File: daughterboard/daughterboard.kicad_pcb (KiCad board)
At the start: 2 copper layers, 150 x 51.8 mm, 15 parts, among them J1 Conn_01x30, J2 Conn_01x02_Female, U1 YAAJ_WeAct_BlackPill_Part_Lik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

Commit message: Daughterboard updates
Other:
- rule pad_to_mask_clearance: 0.0508 -> 0
- board text added: "Daughterboard (Rev 1) Designed by dcpedit github.com/dcpedit/mod-mmm"
- board text removed: "(Rev 1) Designed by dcpedit github.com/dcpedit/mod-mmm"
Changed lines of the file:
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@@
       (dielectric_constraints no)
     )
-    (pad_to_mask_clearance 0.0508)
-    (solder_mask_min_width 0.101)
+    (pad_to_mask_clearance 0)
     (aux_axis_origin 64.77 46.99)
     (grid_origin 64.77 46.99)
@@
       (layerselection 0x00010fc_ffffffff)
       (disableapertmacros false)
-      (usegerberextensions false)
+      (usegerberextensions true)
       (usegerberattributes false)
       (usegerberadvancedattributes false)
@@
       (psa4output false)
       (plotreference true)
-      (plotvalue true)
+      (plotvalue false)
       (plotinvisibletext false)
       (sketchpadsonfab false)
-      (subtractmaskfromsilk false)
+      (subtractmaskfromsilk true)
       (outputformat 1)
       (mirror false)
@@
       (effects (font (size 0.5 0.5) (thickness 0.1)))
     )
-    (fp_text user "REF**" (at 7.62 24.13 90) (layer "F.Fab")
+    (fp_text user "REF**" (at 7.62 24.13 90) (layer "F.Fab") hide
       (effects (font (size 1 1) (thickness 0.15)))
     )
@@
   (gr_arc (start 76.454 96.99) (mid 76.992815 97.213185) (end 77.216 97.752) (layer "Edge.Cuts") (width 0.05))
   (gr_line (start 77.216 97.752) (end 77.216 98.044) (layer "Edge.Cuts") (width 0.05))
-  (gr_text "  (Rev 1)\n Designed by dcpedit\ngithub.com/dcpedit/mod-mmm" (at 154.686 92.583) (layer "F.SilkS")
+  (gr_text "  Daughterboard (Rev 1)\n Designed by dcpedit\ngithub.com/dcpedit/mod-mmm" (at 154.686 92.583) (layer "F.SilkS")
     (effects (font (size 1 1) (thickness 0.15)) (justify left))
   )

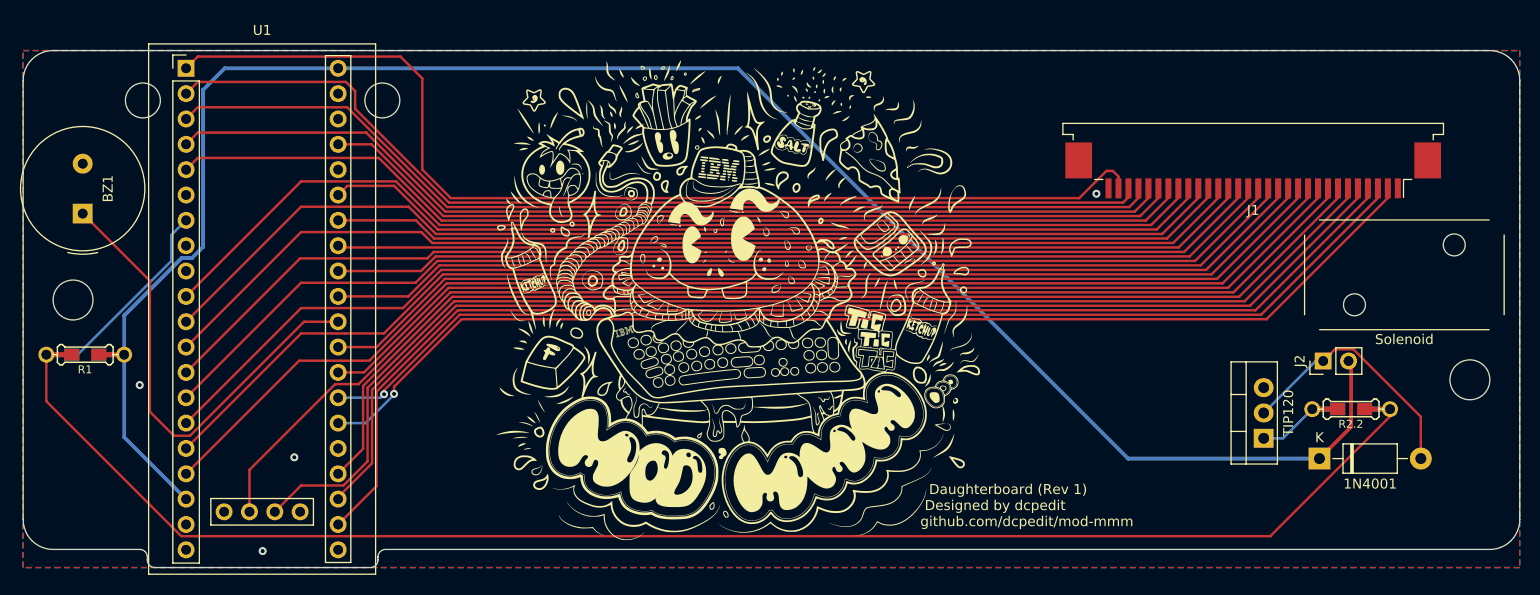
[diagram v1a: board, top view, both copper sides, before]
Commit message: daughterboard rewire
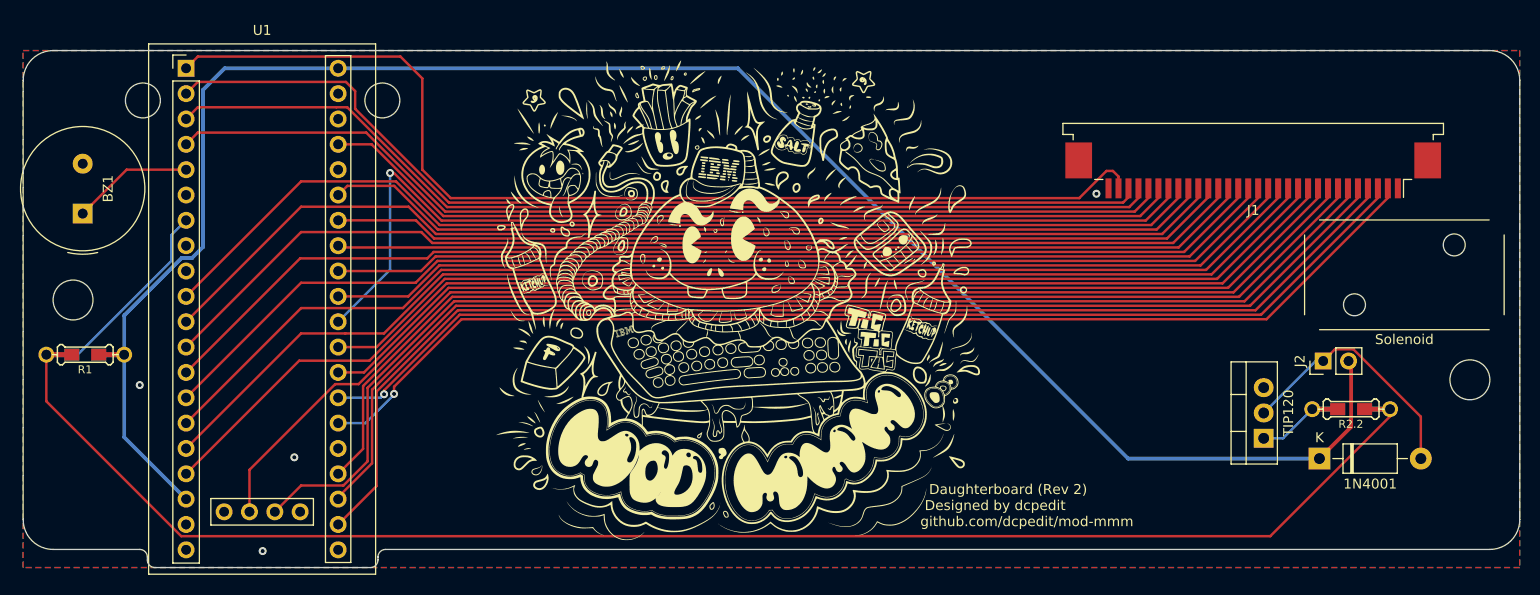
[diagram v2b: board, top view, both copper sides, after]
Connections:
- U1 pad 30: BUZ -> ROW6
- U1 pad 44: /3V3 -> unconnected-(U1-Pad44)
- U1 pad 5: ROW6 -> BUZ
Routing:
- net BUZ: track 47.2 -> 12.2 mm
- net ROW6: track 103.4 -> 98.9 mm, vias 0 -> 1
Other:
- board text added: "Daughterboard (Rev 2) Designed by dcpedit github.com/dcpedit/mod-mmm"
- board text removed: "Daughterboard (Rev 1) Designed by dcpedit github.com/dcpedit/mod-mmm"
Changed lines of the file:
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@@
   (net 1 "GND")
   (net 2 "+5V")
-  (net 3 "Net-(J2-Pad1)")
+  (net 3 "Net-(1N4001-Pad2)")
   (net 4 "BUZ")
   (net 5 "SCRL_LED")
@@
   (net 32 "CAPS_LED")
   (net 33 "SOL")
-  (net 34 "Net-(TIP120-Pad1)")
+  (net 34 "Net-(R2.2-Pad2)")
   (net 35 "unconnected-(U1-Pad38)")
   (net 36 "unconnected-(U1-Pad36)")
@@
   (net 41 "unconnected-(U1-Pad21)")
   (net 42 "unconnected-(U1-Pad20)")
-  (net 43 "/3V3")
+  (net 43 "unconnected-(U1-Pad44)")
   (footprint "MountingHole:MountingHole_3.5mm" locked (layer "F.Cu")
     (at 76.77 51.99)
@@
       (net 2 "+5V") (pinfunction "K") (pintype "passive"))
     (pad "2" thru_hole oval (at 10.16 0) (size 2.2 2.2) (drill 1.1) (layers *.Cu *.Mask)
-      (net 3 "Net-(J2-Pad1)") (pinfunction "A") (pintype "passive"))
+      (net 3 "Net-(1N4001-Pad2)") (pinfunction "A") (pintype "passive"))
     (model "${KICAD6_3DMODEL_DIR}/Diode_THT.3dshapes/D_DO-41_SOD81_P10.16mm_Horizontal.wrl"
       (offset (xyz 0 0 0))
@@
     (fp_line (start -2.46 1.25) (end 7.54 1.25) (layer "F.Fab") (width 0.1))
     (pad "1" thru_hole rect (at 0 0 90) (size 1.905 2) (drill 1.1) (layers *.Cu *.Mask)
-      (net 34 "Net-(TIP120-Pad1)") (pinfunction "B") (pintype "input"))
+      (net 34 "Net-(R2.2-Pad2)") (pinfunction "B") (pintype "input"))
     (pad "2" thru_hole oval (at 2.54 0 90) (size 1.905 2) (drill 1.1) (layers *.Cu *.Mask)
-      (net 3 "Net-(J2-Pad1)") (pinfunction "C") (pintype "passive"))
+      (net 3 "Net-(1N4001-Pad2)") (pinfunction "C") (pintype "passive"))
     (pad "3" thru_hole oval (at 5.08 0 90) (size 1.905 2) (drill 1.1) (layers *.Cu *.Mask)
       (net 1 "GND") (pinfunction "E") (pintype "passive"))
@@
     (fp_line (start -0.635 -1.27) (end 1.27 -1.27) (layer "F.Fab") (width 0.1))
     (pad "1" thru_hole rect (at 0 0 90) (size 1.7 1.7) (drill 1) (layers *.Cu *.Mask)
-      (net 3 "Net-(J2-Pad1)") (pinfunction "Pin_1") (pintype "passive"))
+      (net 3 "Net-(1N4001-Pad2)") (pinfunction "Pin_1") (pintype "passive"))
     (pad "2" thru_hole oval (at 0 2.54 90) (size 1.7 1.7) (drill 1) (layers *.Cu *.Mask)
       (net 2 "+5V") (pinfunction "Pin_2") (pintype "passive"))
@@
       (net 29 "COL2") (pinfunction "PB15") (pintype "bidirectional"))
     (pad "5" thru_hole circle locked (at 0 10.16) (size 1.7 1.7) (drill 1) (layers *.Cu *.Mask)
-      (net 27 "ROW6") (pinfunction "PA8") (pintype "bidirectional"))
+      (net 4 "BUZ") (pinfunction "PA8") (pintype "bidirectional"))
     (pad "6" thru_hole circle locked (at 0 12.7) (size 1.7 1.7) (drill 1) (layers *.Cu *.Mask)
       (net 37 "unconnected-(U1-Pad6)") (pinfunction "PA9") (pintype "bidirectional+no_connect"))
@@
       (net 14 "COL5") (pinfunction "PA3") (pintype "bidirectional"))
     (pad "30" thru_hole circle locked (at 15.24 25.4) (size 1.7 1.7) (drill 1) (layers *.Cu *.Mask)
-      (net 4 "BUZ") (pinfunction "PA4") (pintype "bidirectional"))
+      (net 27 "ROW6") (pinfunction "PA4") (pintype "bidirectional"))
     (pad "31" thru_hole circle locked (at 15.24 22.86) (size 1.7 1.7) (drill 1) (layers *.Cu *.Mask)
       (net 17 "ROW9") (pinfunction "PA5") (pintype "bidirectional"))
@@
       (net 11 "RE2") (pinfunction "SWIO") (pintype "bidirectional"))
     (pad "44" thru_hole circle locked (at 3.812 44.449) (size 1.7 1.7) (drill 1) (layers *.Cu *.Mask)
-      (net 43 "/3V3") (pinfunction "3V3") (pintype "power_in"))
+      (net 43 "unconnected-(U1-Pad44)") (pinfunction "3V3") (pintype "power_in+no_connect"))
     (model "D:/Users/admin/Documents/KiCad/Libraries/packages3d/Modules/STM32_Blue_Pill/YAAJ_BluePill_PinHeaders_H_SWD_cp.wrl"
       (offset (xyz 0 0 0))
@@
       (net 33 "SOL") (pintype "passive") (solder_mask_margin -999))
     (pad "2" smd rect locked (at -2.5 0) (size 2.9 0.5) (layers "B.Cu")
-      (net 34 "Net-(TIP120-Pad1)") (pintype "passive") (solder_mask_margin -999))
+      (net 34 "Net-(R2.2-Pad2)") (pintype "passive") (solder_mask_margin -999))
     (pad "2" smd rect locked (at -1.35 0) (size 1.5 1.2) (layers "F.Cu" "F.Paste" "F.Mask")
-      (net 34 "Net-(TIP120-Pad1)") (pintype "passive"))
+      (net 34 "Net-(R2.2-Pad2)") (pintype "passive"))
     (pad "2" smd rect locked (at -1.35 0) (size 1.5 1.2) (layers "B.Cu" "B.Paste" "B.Mask")
-      (net 34 "Net-(TIP120-Pad1)") (pintype "passive"))
+      (net 34 "Net-(R2.2-Pad2)") (pintype "passive"))
     (pad "2" thru_hole circle locked (at -3.9 0) (size 1.6 1.6) (drill 1) (layers *.Cu *.Mask "F.SilkS")
-      (net 34 "Net-(TIP120-Pad1)") (pintype "passive"))
+      (net 34 "Net-(R2.2-Pad2)") (pintype "passive"))
     (pad "2" smd rect locked (at -2.5 0) (size 2.9 0.5) (layers "F.Cu")
-      (net 34 "Net-(TIP120-Pad1)") (pintype "passive") (solder_mask_margin -999))
+      (net 34 "Net-(R2.2-Pad2)") (pintype "passive") (solder_mask_margin -999))
     (model "${KICAD6_3DMODEL_DIR}/Resistors_SMD.3dshapes/R_0805.step"
       (offset (xyz 0 0 0))
@@
   (gr_arc (start 76.454 96.99) (mid 76.992815 97.213185) (end 77.216 97.752) (layer "Edge.Cuts") (width 0.05))
   (gr_line (start 77.216 97.752) (end 77.216 98.044) (layer "Edge.Cuts") (width 0.05))
-  (gr_text "  Daughterboard (Rev 1)\n Designed by dcpedit\ngithub.com/dcpedit/mod-mmm" (at 154.686 92.583) (layer "F.SilkS")
+  (gr_text "  Daughterboard (Rev 2)\n Designed by dcpedit\ngithub.com/dcpedit/mod-mmm" (at 154.686 92.583) (layer "F.SilkS")
     (effects (font (size 1 1) (thickness 0.15)) (justify left))
   )
@@
   (segment (start 194.31 78.105) (end 195.067 78.105) (width 0.25) (layer "B.Cu") (net 3))
   (segment (start 189.103 83.312) (end 194.31 78.105) (width 0.25) (layer "B.Cu") (net 3))
-  (segment (start 77.47 70.061785) (end 70.739 63.330785) (width 0.25) (layer "F.Cu") (net 4))
-  (segment (start 96.34 74.168) (end 92.92101 74.168) (width 0.25) (layer "F.Cu") (net 4))
-  (segment (start 92.92101 74.168) (end 81.49101 85.598) (width 0.25) (layer "F.Cu") (net 4))
-  (segment (start 79.883 85.598) (end 77.47 83.185) (width 0.25) (layer "F.Cu") (net 4))
-  (segment (start 77.47 83.185) (end 77.47 70.061785) (width 0.25) (layer "F.Cu") (net 4))
-  (segment (start 81.49101 85.598) (end 79.883 85.598) (width 0.25) (layer "F.Cu") (net 4))
+  (segment (start 75.141785 58.928) (end 70.739 63.330785) (width 0.25) (layer "F.Cu") (net 4))
+  (segment (start 81.1 58.928) (end 75.141785 58.928) (width 0.25) (layer "F.Cu") (net 4))
   (segment (start 201.55 61.754022) (end 201.55 60.8) (width 0.25) (layer "F.Cu") (net 5))
   (segment (start 189.386503 73.917519) (end 201.55 61.754022) (width 0.25) (layer "F.Cu") (net 5))
@@
   (segment (start 177.826422 64.4776) (end 180.55 61.754022) (width 0.25) (layer "F.Cu") (net 26))
   (segment (start 106.512449 64.4776) (end 177.826422 64.4776) (width 0.25) (layer "F.Cu") (net 26))
-  (segment (start 177.275942 64.02808) (end 179.55 61.754022) (width 0.25) (layer "F.Cu") (net 27))
-  (segment (start 82.274511 57.753489) (end 100.424053 57.753489) (width 0.25) (layer "F.Cu") (net 27))
-  (segment (start 81.1 58.928) (end 82.274511 57.753489) (width 0.25) (layer "F.Cu") (net 27))
-  (segment (start 106.698646 64.02808) (end 177.275942 64.02808) (width 0.25) (layer "F.Cu") (net 27))
-  (segment (start 100.424053 57.753489) (end 106.698646 64.02808) (width 0.25) (layer "F.Cu") (net 27))
+  (segment (start 101.543609 59.261924) (end 101.932488 59.261924) (width 0.25) (layer "F.Cu") (net 27))
   (segment (start 179.55 61.754022) (end 179.55 60.8) (width 0.25) (layer "F.Cu") (net 27))
+  (segment (start 106.698646 64.02808) (end 177.275942 64.02808) (width 0.25) (layer "F.Cu") (net 27))
+  (segment (start 177.275942 64.02808) (end 179.55 61.754022) (width 0.25) (layer "F.Cu") (net 27))
+  (segment (start 101.932488 59.261924) (end 106.698646 64.02808) (width 0.25) (layer "F.Cu") (net 27))
+  (via (at 101.543609 59.261924) (size 0.8) (drill 0.4) (layers "F.Cu" "B.Cu") (net 27))
+  (segment (start 96.34 74.168) (end 101.543609 68.964391) (width 0.25) (layer "B.Cu") (net 27))
+  (segment (start 101.543609 68.964391) (end 101.543609 59.261924) (width 0.25) (layer "B.Cu") (net 27))
   (segment (start 99.694282 56.388) (end 106.884843 63.57856) (width 0.25) (layer "F.Cu") (net 28))
   (segment (start 106.884843 63.57856) (end 176.725462 63.57856) (width 0.25) (layer "F.Cu") (net 28))

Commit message: v3 with 10u support
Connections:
- U1 pad 41: GND -> unconnected-(U1-Pad41)
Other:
- board text added: "Daughterboard (Rev 2.1) Designed by dcpedit github.com/dcpedit/mod-mmm"
- board text removed: "Daughterboard (Rev 2) Designed by dcpedit github.com/dcpedit/mod-mmm"
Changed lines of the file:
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@@
   (net 42 "unconnected-(U1-Pad20)")
   (net 43 "unconnected-(U1-Pad44)")
+  (net 44 "unconnected-(U1-Pad41)")
   (footprint "MountingHole:MountingHole_3.5mm" locked (layer "F.Cu")
     (at 76.77 51.99)
@@
       (net 2 "+5V") (pinfunction "5V") (pintype "power_in"))
     (pad "41" thru_hole circle locked (at 11.432 44.449) (size 1.7 1.7) (drill 1) (layers *.Cu *.Mask)
-      (net 1 "GND") (pinfunction "GND") (pintype "power_in"))
+      (net 44 "unconnected-(U1-Pad41)") (pinfunction "GND") (pintype "power_in+no_connect"))
     (pad "42" thru_hole circle locked (at 8.892 44.449) (size 1.7 1.7) (drill 1) (layers *.Cu *.Mask)
       (net 9 "RE3") (pinfunction "SWCLK") (pintype "bidirectional"))
@@
   (gr_arc (start 76.454 96.99) (mid 76.992815 97.213185) (end 77.216 97.752) (layer "Edge.Cuts") (width 0.05))
   (gr_line (start 77.216 97.752) (end 77.216 98.044) (layer "Edge.Cuts") (width 0.05))
-  (gr_text "  Daughterboard (Rev 2)\n Designed by dcpedit\ngithub.com/dcpedit/mod-mmm" (at 154.686 92.583) (layer "F.SilkS")
+  (gr_text "  Daughterboard (Rev 2.1)\n Designed by dcpedit\ngithub.com/dcpedit/mod-mmm" (at 154.686 92.583) (layer "F.SilkS")
     (effects (font (size 1 1) (thickness 0.15)) (justify left))
   )

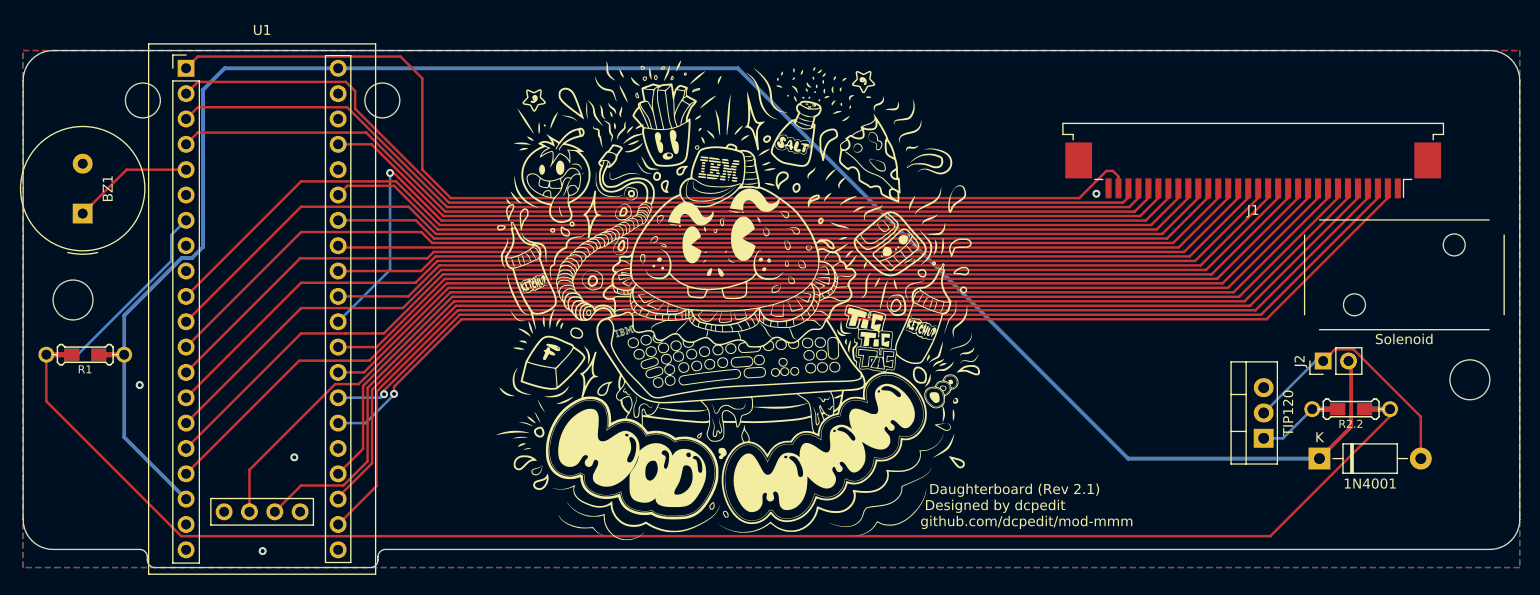
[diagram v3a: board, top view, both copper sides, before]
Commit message: Fix ortho diode
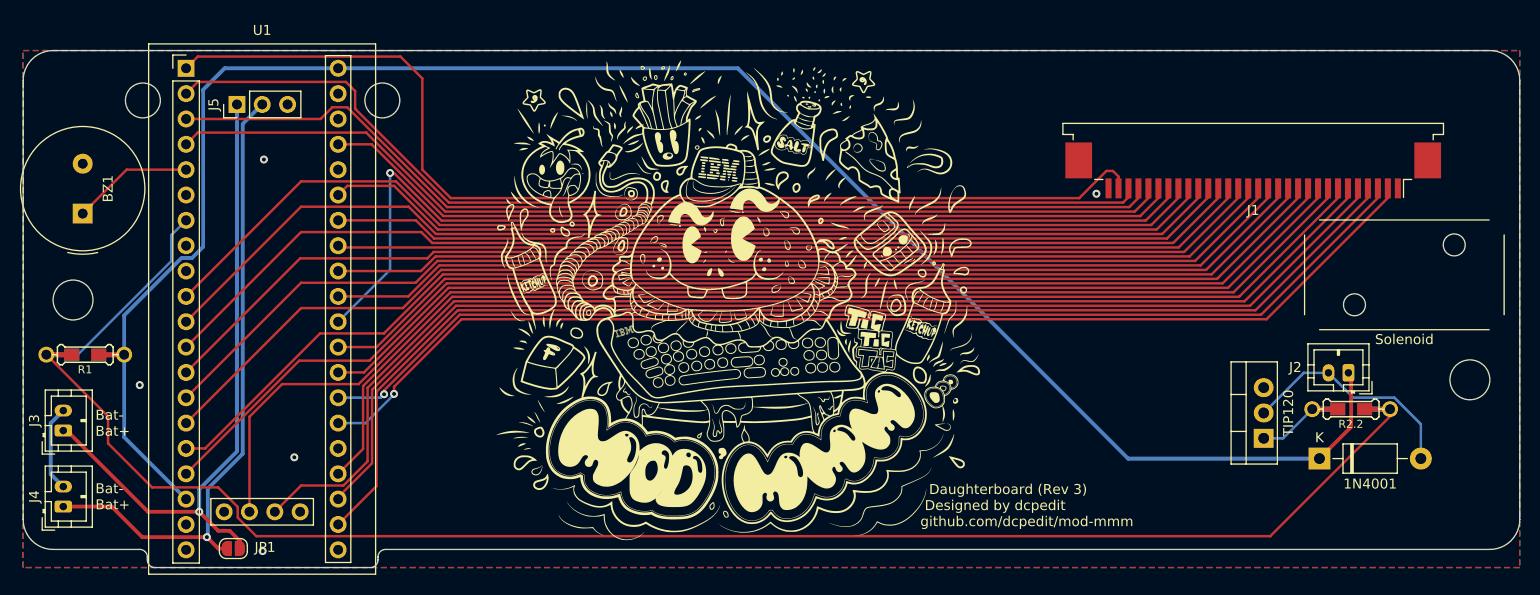
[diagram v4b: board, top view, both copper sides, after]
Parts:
- added J3: Bat_in, Connector_JST:JST_PH_B2B-PH-K_1x02_P2.00mm_Vertical, F.Cu at (68.8, 85.1)
- added J4: Bat_out, Connector_JST:JST_PH_B2B-PH-K_1x02_P2.00mm_Vertical, F.Cu at (68.8, 92.7)
- added J5: PWR_switch, Connector_PinHeader_2.54mm:PinHeader_1x03_P2.54mm_Vertical, F.Cu at (86.2, 52.4)
- added JP1: Switch_bypass, Jumper:SolderJumper-2_P1.3mm_Open_RoundedPad1.0x1.5mm, F.Cu at (85.8, 96.9)
- J2: value Conn_01x02_Female -> Conn_sol; footprint Connector_PinHeader_2.54mm:PinHeader_1x02_P2.54mm_Vertical -> Connector_JST:JST_PH_B2B-PH-K_1x02_P2.00mm_Vertical
- moved J2 2.79 mm to (197.6, 79.3), turned to 180 degrees
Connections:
- 1N4001 pad 2: Net-(1N4001-Pad2) -> Net-(1N4001-A)
- J2 pad 1: Net-(1N4001-Pad2) -> +5V
- J2 pad 2: +5V -> Net-(1N4001-A)
- TIP120 pad 2: Net-(1N4001-Pad2) -> Net-(1N4001-A)
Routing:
- net BAT_R: track 0.00 -> 65.4 mm, vias 0 -> 1
- net BAT_RR: track 0.00 -> 63.8 mm, vias 0 -> 1
- net Net-(1N4001-Pad2): track 25.4 -> 0.00 mm
- net Net-(1N4001-A): track 0.00 -> 23.0 mm
- net BAT_B: track 0.00 -> 8.67 mm
- net RE2: track 124.5 -> 127.7 mm
- net +5V: track 187.7 -> 186.5 mm
- net SOL: track 169.2 -> 168.7 mm
- net GND: vias 4 -> 5
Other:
- board text added: "Bat- Bat+"
- board text added: "Daughterboard (Rev 3) Designed by dcpedit github.com/dcpedit/mod-mmm"
- board text removed: "Daughterboard (Rev 2.1) Designed by dcpedit github.com/dcpedit/mod-mmm"
